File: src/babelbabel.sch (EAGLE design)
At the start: 86 parts, among them CON1 CON-4P-TABS-JST_GH-RA, CON10 CON-6P-SM06B, CON11 PINHEAD_1X04-2.54, CON12 PINHEAD_1X06-2.54, CON15 PINHEAD_1X04-2.54, CON16 CON-4P-TABS-JST_GH-RA, CON2 PINHEAD_1X04-2.54, CON3 PINHEAD_1X04-2.54, CON4 USB-AA-PTH, CON5 CON-4P-TABS-JST_GH-RA, CON6 CON-4P-TABS-JST_GH-RA, CON7 USB-1, IC1 NS5B1G385, IC13 STM32F103CBT7, IC14 74LVC2T45, IC15 74LVC2T45, IC16 74LVC2T45, IC17 74LVC2T45, IC2 NS5B1G385, IC3 AP2127-3.3, IC9 FE1.1S, J1 CONNECTION-SMD, J2 CONNECTION-SMD, Q7 8MHz, Q8 12MHz, Q9 NTZD3152PT1G

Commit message: removed unnecessary assembly variant
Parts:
- removed S1, S3: DS01-STRAIGHT, misc:DS01-STRAIGHT
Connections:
- net CANH1: no longer S1.1
- net CANH2: no longer S3.1
- net CAN_L: no longer S1.10
- net N$2: no longer S3.10

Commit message: changed footprint CON4 (#21)
* changed footprint CON4

* fixed wrong USB connection
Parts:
- CON4: LCSC# C39437 -> (none)
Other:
- moved on the sheet: CON4
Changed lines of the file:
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@@
 <part name="+P2" library="supply_symbols" library_urn="urn:adsk.eagle:library:5017758" deviceset="5V" device=""/>
 <part name="+P3" library="supply_symbols" library_urn="urn:adsk.eagle:library:5017758" deviceset="3.3V" device=""/>
-<part name="CON4" library="Connectors" library_urn="urn:adsk.eagle:library:3750510" deviceset="USB-A" device="A-PTH" package3d_urn="urn:adsk.eagle:package:25290692/2">
-<attribute name="LCSC#" value="C39437"/>
-</part>
 <part name="GND3" library="supply_symbols" library_urn="urn:adsk.eagle:library:5017758" deviceset="GND" device="" value="GND"/>
 <part name="+P4" library="supply_symbols" library_urn="urn:adsk.eagle:library:5017758" deviceset="5V" device=""/>
@@
 </part>
 <part name="GND25" library="supply_symbols" library_urn="urn:adsk.eagle:library:5017758" deviceset="GND" device="" value="GND"/>
+<part name="CON4" library="Connectors" deviceset="USB-A" device="A-PTH"/>
 </parts>
 <sheets>
@@
 <attribute name="VALUE" x="20.32" y="171.196" size="1.27" layer="96" font="vector" ratio="15" align="center"/>
 </instance>
-<instance part="CON4" gate="G$1" x="111.76" y="106.68" smashed="yes" rot="MR180">
-<attribute name="NAME" x="114.3" y="92.71" size="1.778" layer="95" font="vector" ratio="15" rot="MR180" align="center"/>
-<attribute name="MANF#" x="114.3" y="107.95" size="1.778" layer="95" font="vector" ratio="15" rot="MR180" align="center"/>
-<attribute name="LCSC#" x="111.76" y="106.68" size="1.778" layer="96" rot="MR180" display="off"/>
-</instance>
 <instance part="GND3" gate="1" x="106.68" y="71.12" smashed="yes">
 <attribute name="VALUE" x="106.68" y="69.85" size="1.27" layer="96" font="vector" ratio="15" align="center"/>
@@
 <instance part="GND25" gate="1" x="134.62" y="38.1" smashed="yes">
 <attribute name="VALUE" x="134.62" y="36.83" size="1.27" layer="96" font="vector" ratio="15" align="center"/>
+</instance>
+<instance part="CON4" gate="G$1" x="114.3" y="109.22" smashed="yes" rot="MR180">
+<attribute name="NAME" x="116.84" y="95.25" size="1.778" layer="95" font="vector" ratio="15" rot="MR180" align="center"/>
+<attribute name="MANF#" x="116.84" y="110.49" size="1.778" layer="95" font="vector" ratio="15" rot="MR180" align="center"/>
 </instance>
 </instances>
@@
 </segment>
 <segment>
-<pinref part="CON4" gate="G$1" pin="GND"/>
 <pinref part="CON15" gate="G$1" pin="4"/>
-<wire x1="106.68" y1="104.14" x2="109.22" y2="104.14" width="0.1524" layer="91"/>
 <wire x1="109.22" y1="83.82" x2="106.68" y2="83.82" width="0.1524" layer="91"/>
-<wire x1="106.68" y1="83.82" x2="106.68" y2="104.14" width="0.1524" layer="91"/>
 <pinref part="GND3" gate="1" pin="GND"/>
 <wire x1="106.68" y1="73.66" x2="106.68" y2="83.82" width="0.1524" layer="91"/>
-<junction x="106.68" y="83.82"/>
+<wire x1="106.68" y1="73.66" x2="106.68" y2="106.68" width="0.1524" layer="91"/>
+<junction x="106.68" y="73.66"/>
+<pinref part="CON4" gate="G$1" pin="GND"/>
+<wire x1="106.68" y1="106.68" x2="111.76" y2="106.68" width="0.1524" layer="91"/>
 </segment>
 <segment>
@@
 <net name="DUT_DP" class="0">
 <segment>
-<pinref part="CON4" gate="G$1" pin="D+"/>
 <pinref part="CON15" gate="G$1" pin="3"/>
-<wire x1="104.14" y1="101.6" x2="109.22" y2="101.6" width="0.1524" layer="91"/>
 <wire x1="109.22" y1="81.28" x2="104.14" y2="81.28" width="0.1524" layer="91"/>
-<wire x1="104.14" y1="81.28" x2="104.14" y2="101.6" width="0.1524" layer="91"/>
 <pinref part="IC9" gate="G$1" pin="DP1"/>
 <wire x1="83.82" y1="134.62" x2="104.14" y2="134.62" width="0.1524" layer="91"/>
-<wire x1="104.14" y1="134.62" x2="104.14" y2="101.6" width="0.1524" layer="91"/>
-<junction x="104.14" y="101.6"/>
+<wire x1="104.14" y1="134.62" x2="104.14" y2="104.14" width="0.1524" layer="91"/>
+<pinref part="CON4" gate="G$1" pin="D+"/>
+<wire x1="104.14" y1="104.14" x2="104.14" y2="81.28" width="0.1524" layer="91"/>
+<wire x1="111.76" y1="104.14" x2="104.14" y2="104.14" width="0.1524" layer="91"/>
+<junction x="104.14" y="104.14"/>
 </segment>
 </net>
 <net name="DUT_DM" class="0">
 <segment>
+<pinref part="CON15" gate="G$1" pin="2"/>
+<wire x1="109.22" y1="78.74" x2="101.6" y2="78.74" width="0.1524" layer="91"/>
+<pinref part="IC9" gate="G$1" pin="DM1"/>
+<wire x1="101.6" y1="78.74" x2="101.6" y2="101.6" width="0.1524" layer="91"/>
+<wire x1="101.6" y1="101.6" x2="101.6" y2="132.08" width="0.1524" layer="91"/>
+<wire x1="101.6" y1="132.08" x2="83.82" y2="132.08" width="0.1524" layer="91"/>
 <pinref part="CON4" gate="G$1" pin="D-"/>
-<pinref part="CON15" gate="G$1" pin="2"/>
-<wire x1="101.6" y1="99.06" x2="109.22" y2="99.06" width="0.1524" layer="91"/>
-<wire x1="109.22" y1="78.74" x2="101.6" y2="78.74" width="0.1524" layer="91"/>
-<wire x1="101.6" y1="78.74" x2="101.6" y2="99.06" width="0.1524" layer="91"/>
-<pinref part="IC9" gate="G$1" pin="DM1"/>
-<wire x1="101.6" y1="99.06" x2="101.6" y2="132.08" width="0.1524" layer="91"/>
-<wire x1="101.6" y1="132.08" x2="83.82" y2="132.08" width="0.1524" layer="91"/>
-<junction x="101.6" y="99.06"/>
+<wire x1="111.76" y1="101.6" x2="101.6" y2="101.6" width="0.1524" layer="91"/>
+<junction x="101.6" y="101.6"/>
 </segment>
 </net>
@@
 </segment>
 <segment>
+<pinref part="+P4" gate="G$1" pin="VDD_5V"/>
+<pinref part="CON15" gate="G$1" pin="1"/>
+<wire x1="109.22" y1="76.2" x2="99.06" y2="76.2" width="0.1524" layer="91"/>
+<wire x1="99.06" y1="76.2" x2="99.06" y2="99.06" width="0.1524" layer="91"/>
 <pinref part="CON4" gate="G$1" pin="VBUS"/>
-<pinref part="+P4" gate="G$1" pin="VDD_5V"/>
-<wire x1="109.22" y1="96.52" x2="99.06" y2="96.52" width="0.1524" layer="91"/>
-<pinref part="CON15" gate="G$1" pin="1"/>
-<wire x1="99.06" y1="96.52" x2="99.06" y2="99.06" width="0.1524" layer="91"/>
-<wire x1="109.22" y1="76.2" x2="99.06" y2="76.2" width="0.1524" layer="91"/>
-<wire x1="99.06" y1="76.2" x2="99.06" y2="96.52" width="0.1524" layer="91"/>
-<junction x="99.06" y="96.52"/>
-</segment>
-<segment>
+<wire x1="99.06" y1="99.06" x2="111.76" y2="99.06" width="0.1524" layer="91"/>
+<junction x="99.06" y="99.06"/>
+</segment>
+<segment>

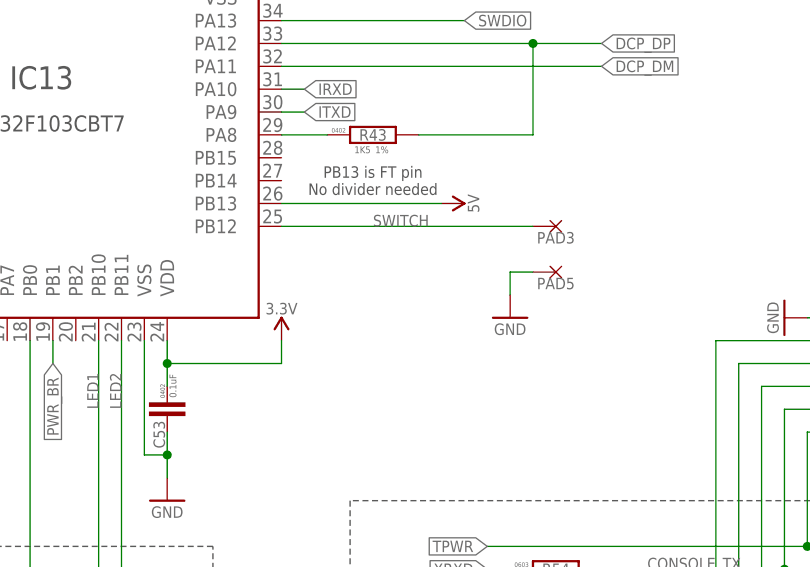
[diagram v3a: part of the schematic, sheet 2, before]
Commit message: DCP switch pulled high
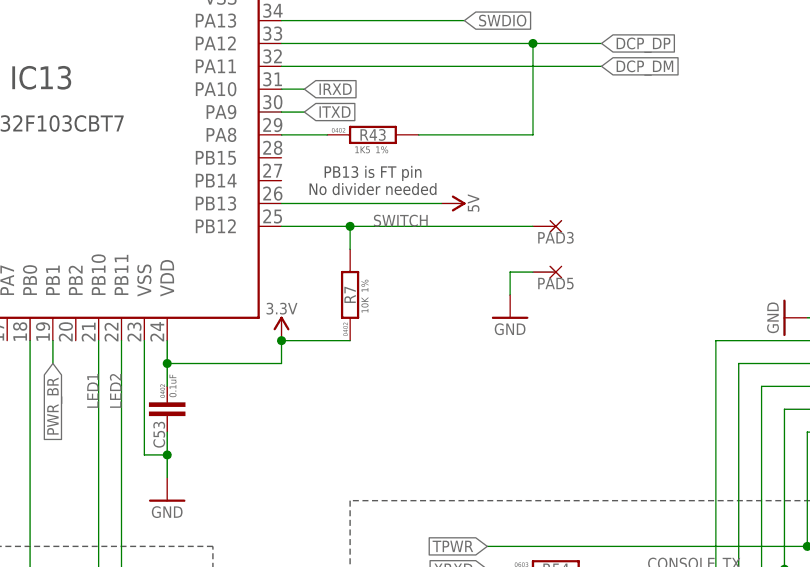
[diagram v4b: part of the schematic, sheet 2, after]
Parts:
- added R7: 10K, rc:R-1%-0402
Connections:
- net SWITCH: now also R7.2
- net VDD_3V3: now also R7.1
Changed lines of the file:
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@@
 <part name="GND25" library="supply_symbols" library_urn="urn:adsk.eagle:library:5017758" deviceset="GND" device="" value="GND"/>
 <part name="CON4" library="Connectors" deviceset="USB-A" device="A-PTH"/>
+<part name="R7" library="rc" library_urn="urn:adsk.eagle:library:2539423" deviceset="R" device="-0402" package3d_urn="urn:adsk.eagle:package:2539456/2" technology="-1%" value="10K">
+<attribute name="LCSC#" value="C25744"/>
+</part>
 </parts>
 <sheets>
@@
 <attribute name="VALUE" x="114.3" y="95.25" size="1.27" layer="96" font="vector" ratio="15" align="center"/>
 </instance>
+<instance part="R7" gate="G$1" x="96.52" y="99.06" smashed="yes" rot="R90">
+<attribute name="NAME" x="96.52" y="99.06" size="1.27" layer="95" font="vector" rot="R90" align="center"/>
+<attribute name="VALUE" x="98.552" y="98.806" size="0.762" layer="96" font="vector" rot="R90" align="bottom-right"/>
+<attribute name="PACKAGE" x="96.012" y="95.25" size="0.508" layer="95" font="vector" rot="R90" align="center"/>
+<attribute name="TOLERANCE" x="98.552" y="99.314" size="0.762" layer="96" font="vector" rot="R90"/>
+</instance>
 </instances>
 <busses>
@@
 <pinref part="IC13" gate="G$1" pin="PB12"/>
 <pinref part="PAD3" gate="G$1" pin="P$1"/>
-<wire x1="88.9" y1="106.68" x2="116.84" y2="106.68" width="0.1524" layer="91"/>
+<wire x1="88.9" y1="106.68" x2="96.52" y2="106.68" width="0.1524" layer="91"/>
 <label x="99.06" y="106.68" size="1.27" layer="95" font="vector"/>
+<pinref part="R7" gate="G$1" pin="2"/>
+<wire x1="96.52" y1="106.68" x2="116.84" y2="106.68" width="0.1524" layer="91"/>
+<wire x1="96.52" y1="104.14" x2="96.52" y2="106.68" width="0.1524" layer="91"/>
+<junction x="96.52" y="106.68"/>
 </segment>
 </net>
@@
 <wire x1="88.9" y1="91.44" x2="76.2" y2="91.44" width="0.1524" layer="91"/>
 <junction x="76.2" y="91.44"/>
-</segment>
-<segment>
+<pinref part="R7" gate="G$1" pin="1"/>
+<wire x1="96.52" y1="93.98" x2="88.9" y2="93.98" width="0.1524" layer="91"/>
+<junction x="88.9" y="93.98"/>
+</segment>
+<segment>
